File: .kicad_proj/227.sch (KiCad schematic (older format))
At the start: 6 parts, among them U1 ATmega328-PU, U2 MC7905

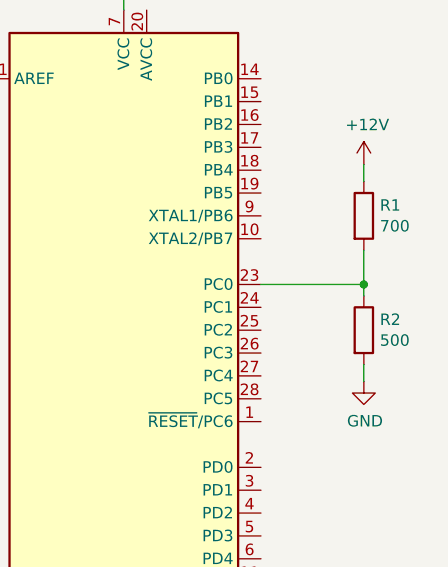
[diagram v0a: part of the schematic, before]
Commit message: Finish 2.2.3, change R values in 2.2.7, change 3-state switch component in 2.2.2
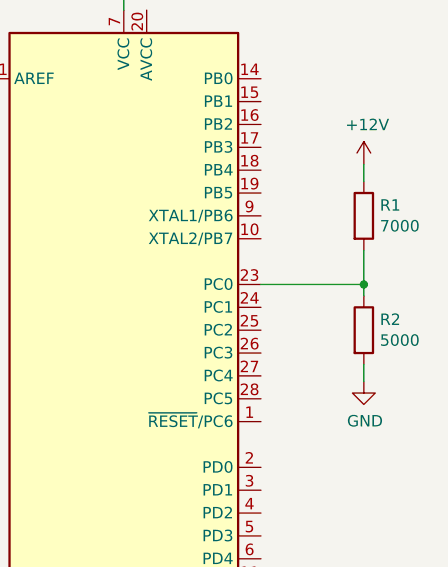
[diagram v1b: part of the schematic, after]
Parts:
- R1: value 700 -> 7000
- R2: value 500 -> 5000
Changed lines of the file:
@@
 P 6075 3050
 F 0 "R1" H 6145 3096 50  0000 L CNN
-F 1 "700" H 6145 3005 50  0000 L CNN
+F 1 "7000" H 6145 3005 50  0000 L CNN
 F 2 "" V 6005 3050 50  0001 C CNN
 F 3 "~" H 6075 3050 50  0001 C CNN
@@
 P 6075 3550
 F 0 "R2" H 6145 3596 50  0000 L CNN
-F 1 "500" H 6145 3505 50  0000 L CNN
+F 1 "5000" H 6145 3505 50  0000 L CNN
 F 2 "" V 6005 3550 50  0001 C CNN
 F 3 "~" H 6075 3550 50  0001 C CNN

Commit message: Add schematics 9, 10, 11 and 12
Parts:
- R1: value 7000 -> 7k
- R2: value 5000 -> 5k
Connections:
- net at C2.1, U1.7 (VCC), U2.2 (VI): now also U1.20 (AVCC)
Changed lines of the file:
@@
 $Descr A4 11693 8268
 encoding utf-8
-Sheet 8 9
+Sheet 8 19
 Title ""
 Date ""
@@
 P 6075 3050
 F 0 "R1" H 6145 3096 50  0000 L CNN
-F 1 "7000" H 6145 3005 50  0000 L CNN
+F 1 "7k" H 6145 3005 50  0000 L CNN
 F 2 "" V 6005 3050 50  0001 C CNN
 F 3 "~" H 6075 3050 50  0001 C CNN
@@
 P 6075 3550
 F 0 "R2" H 6145 3596 50  0000 L CNN
-F 1 "5000" H 6145 3505 50  0000 L CNN
+F 1 "5k" H 6145 3505 50  0000 L CNN
 F 2 "" V 6005 3550 50  0001 C CNN
 F 3 "~" H 6075 3550 50  0001 C CNN
@@
 Wire Wire Line
 	5625 3350 6075 3350
+Wire Wire Line
+	5125 2150 5025 2150
+Connection ~ 5025 2150
 $EndSCHEMATC
